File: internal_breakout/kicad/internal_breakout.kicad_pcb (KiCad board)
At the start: 2 copper layers, 50 x 35 mm, 27 parts, among them J1 MA03-1, J10 2X5, J11 2X5, J12 MA03-1, J13 MA03-1, J14 MA03-1, J15 MA03-1, J16 MA03-1, J17 MA03-1, J18 Conn_02x01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

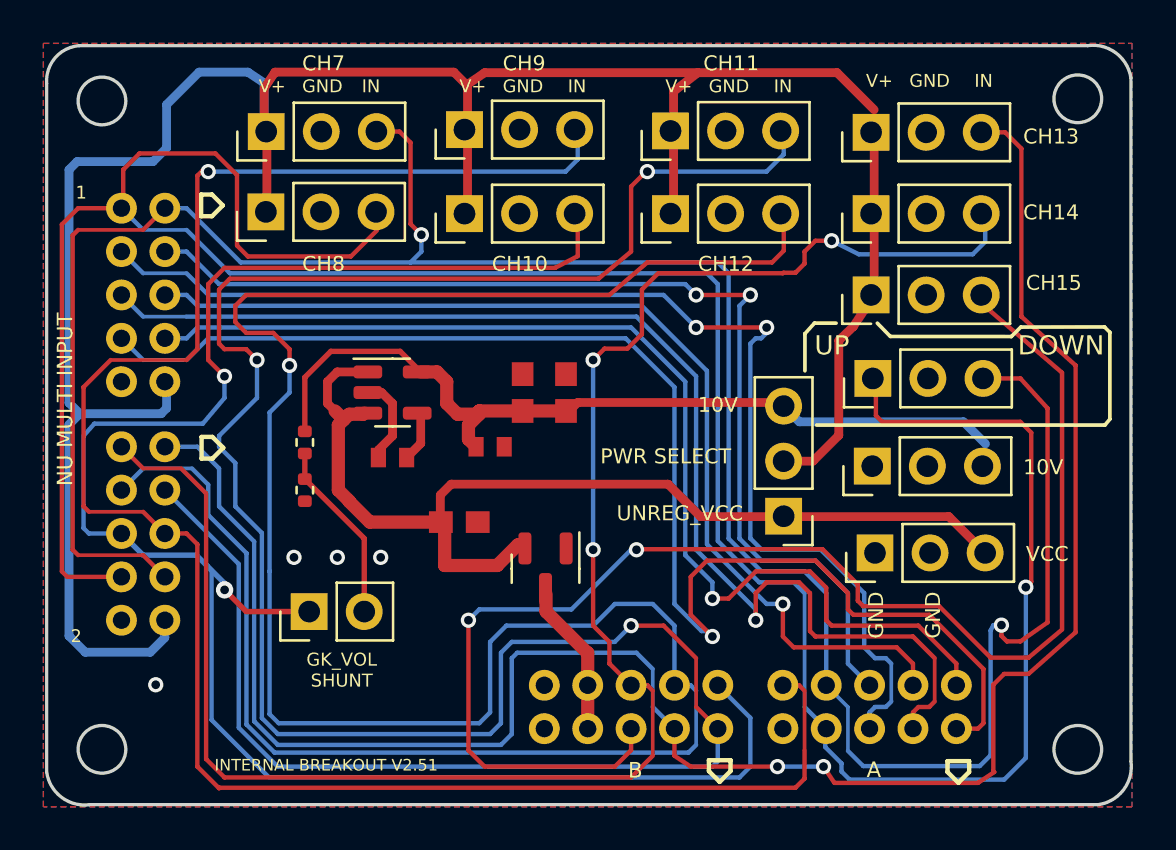
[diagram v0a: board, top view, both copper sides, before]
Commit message: Perfect port to KiCAD
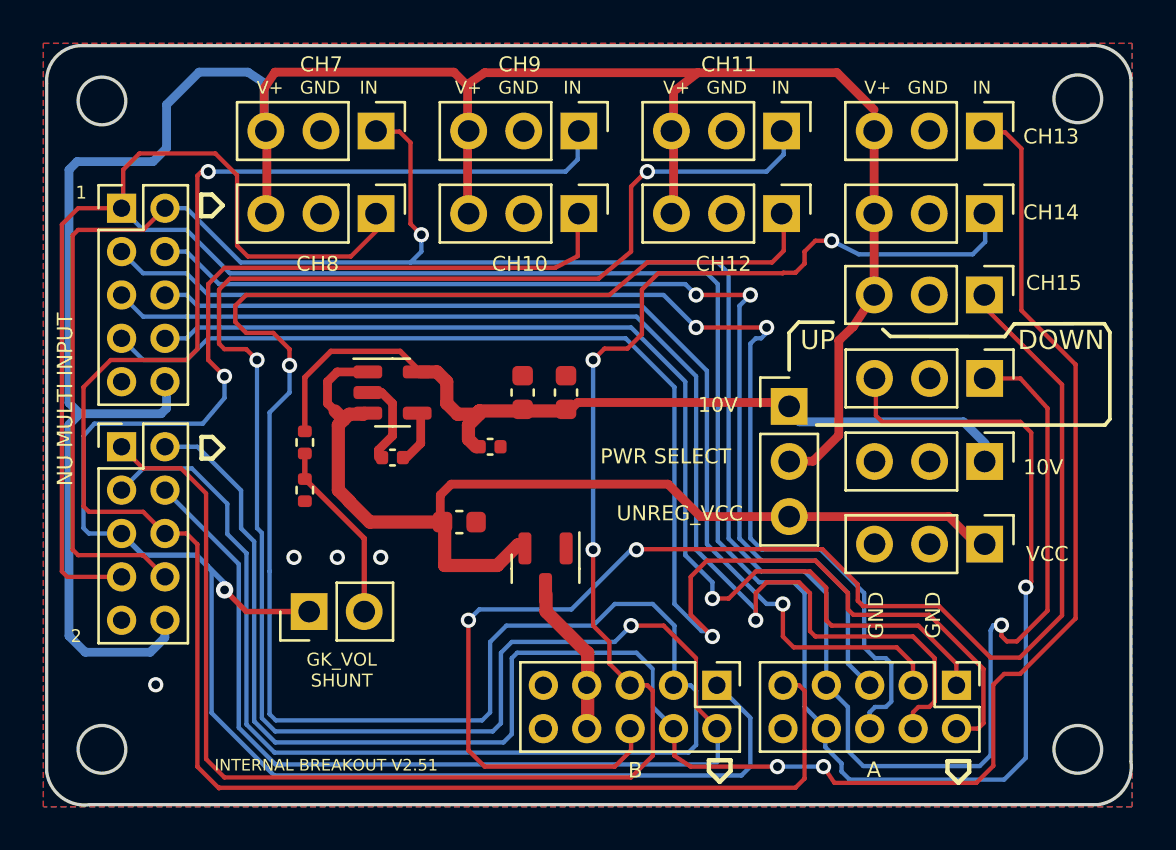
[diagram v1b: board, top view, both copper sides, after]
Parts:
- C1, C2: value C-EUC0603 -> 10uF; footprint internal_breakout:C0603 -> Capacitor_SMD:C_0603_1608Metric
- C3: value C-EUC0603 -> 1uF; footprint internal_breakout:C0603 -> Capacitor_SMD:C_0603_1608Metric
- C4: value C-EUC0402 -> 10nF; footprint internal_breakout:C0402 -> Capacitor_SMD:C_0402_1005Metric
- C5: value C-EUC0402 -> 100nF; footprint internal_breakout:C0402 -> Capacitor_SMD:C_0402_1005Metric
- J10, J11, J3, J4: footprint internal_breakout:2X5 -> Connector_PinHeader_2.00mm:PinHeader_2x05_P2.00mm_Vertical; moved to F.Cu
- J15, J16, J17: value MA03-1 -> Conn_01x03
- R1, R2: value R_Small -> 50K
- U1: value LP2985AIM5-3.3 -> LP2985-10DBVR
- moved J1 5.27 mm to (148.0, 91.4), turned to -90 degrees
- moved J2 5.27 mm to (148.0, 95.2), turned to -90 degrees
- moved J8 5.22 mm to (166.7, 91.4), turned to -90 degrees
- moved J7 5.22 mm to (166.7, 95.2), turned to -90 degrees
- moved J9 5.22 mm to (166.7, 99.0), turned to -90 degrees
- moved J12 5.19 mm to (166.8, 106.7), turned to -90 degrees
- moved J17 5.16 mm to (166.8, 102.8), turned to -90 degrees
- moved J6 5.12 mm to (157.4, 91.4), turned to -90 degrees
- moved J5 5.12 mm to (157.4, 95.2), turned to -90 degrees
- moved J16 5.08 mm to (138.7, 95.2), turned to -90 degrees
- moved J13 5.07 mm to (166.8, 110.5), turned to -90 degrees
- moved J14 5.07 mm to (157.7, 104.1), turned to 0 degrees
- moved J15 5.07 mm to (138.7, 91.4), turned to -90 degrees
- moved J10 4.13 mm to (165.4, 117.0), turned to -90 degrees
- moved J3 4.12 mm to (127.0, 95.0), turned to 0 degrees
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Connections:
- net /CH1 renamed CH2
- net /CH2 renamed CH1
- net /CH3 renamed CH4
- net /CH4 renamed CH3
- net /CH5 renamed CH6
- net /CH6 renamed CH5
- net /VIN renamed VIN
- C1 pad 1: /VCC -> VCC
- C2 pad 1: /+10VA -> +10VA
- C3 pad 1: /+10VA -> +10VA
- C5 pad 1: /+10VA -> +10VA
- J1 pad 1: /V+ -> CH9
- J1 pad 3: /CH9 -> V+
- J10 pad 10: /CH9 -> GND
- J10 pad 7: /CH8 -> CH7
- J10 pad 8: /CH7 -> CH8
- J10 pad 9: GND -> CH9
- J11 pad 1: /CH11 -> CH10
- J11 pad 2: /CH10 -> CH11
- J11 pad 3: /CH13 -> CH12
- J11 pad 4: /CH12 -> CH13
- J11 pad 5: /CH15 -> CH14
- J11 pad 6: /CH14 -> CH15
- J12 pad 1: GND -> +10VA
- J12 pad 3: /+10VA -> GND
- J13 pad 1: GND -> VCC
- J13 pad 3: /VCC -> GND
- J14 pad 1: /VCC -> +10VA
- J14 pad 2: /V+ -> V+
- J14 pad 3: /+10VA -> VCC
- J15 pad 1: /V+ -> CH7
- J15 pad 3: /CH7 -> V+
- J16 pad 1: /V+ -> CH8
- J16 pad 3: /CH8 -> V+
- J17 pad 1: /CH8 -> CH7
- J17 pad 3: /CH7 -> CH8
- J18 pad 1: /CH10 -> CH10
- J2 pad 1: /V+ -> CH10
- J2 pad 3: /CH10 -> V+
- J3 pad 1: /CH7 -> CH8
- J3 pad 10: GND -> V+
- J3 pad 2: /CH8 -> CH7
- J3 pad 9: /V+ -> GND
- J4 pad 1: /CH13 -> CH14
- J4 pad 10: GND -> V+
- J4 pad 2: /CH14 -> CH13
- J4 pad 3: /CH11 -> CH12
- J4 pad 4: /CH12 -> CH11
- J4 pad 5: /CH9 -> CH10
- J4 pad 6: /CH10 -> CH9
- J4 pad 7: /CH7 -> CH8
- J4 pad 8: /CH8 -> CH7
- J4 pad 9: /V+ -> GND
- J5 pad 1: /V+ -> CH12
- J5 pad 3: /CH12 -> V+
- J6 pad 1: /V+ -> CH11
- J6 pad 3: /CH11 -> V+
- J7 pad 1: /V+ -> CH14
- J7 pad 3: /CH14 -> V+
- J8 pad 1: /V+ -> CH13
- J8 pad 3: /CH13 -> V+
- J9 pad 1: /V+ -> CH15
- J9 pad 3: /CH15 -> V+
- Q1 pad 2: /VCC -> VCC
- R1 pad 1: /+10VA -> +10VA
- U1 pad 1: /VCC -> VCC
- U1 pad 3: /VCC -> VCC
- U1 pad 5: /+10VA -> +10VA
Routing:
- net CH8: track 0.00 -> 128.1 mm, vias 0 -> 1
- net /CH8: track 128.1 -> 0.00 mm, vias 1 -> 0
- net /CH11: track 119.4 -> 0.00 mm, vias 3 -> 0
- net CH11: track 0.00 -> 117.8 mm, vias 0 -> 3
- net /CH12: track 116.7 -> 0.00 mm, vias 1 -> 0
- net CH12: track 0.00 -> 116.6 mm, vias 0 -> 1
- net /CH7: track 114.2 -> 0.00 mm, vias 2 -> 0
- net CH7: track 0.00 -> 114.0 mm, vias 0 -> 2
- net V+: track 0.00 -> 113.1 mm
- net /V+: track 113.1 -> 0.00 mm
- net /CH13: track 92.3 -> 0.00 mm, vias 2 -> 0
- net CH13: track 0.00 -> 91.6 mm, vias 0 -> 2
- net CH9: track 0.00 -> 88.7 mm, vias 0 -> 1
- net /CH9: track 88.7 -> 0.00 mm, vias 1 -> 0
- net /CH10: track 86.4 -> 0.00 mm, vias 2 -> 0
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
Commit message: LCSC part numbers
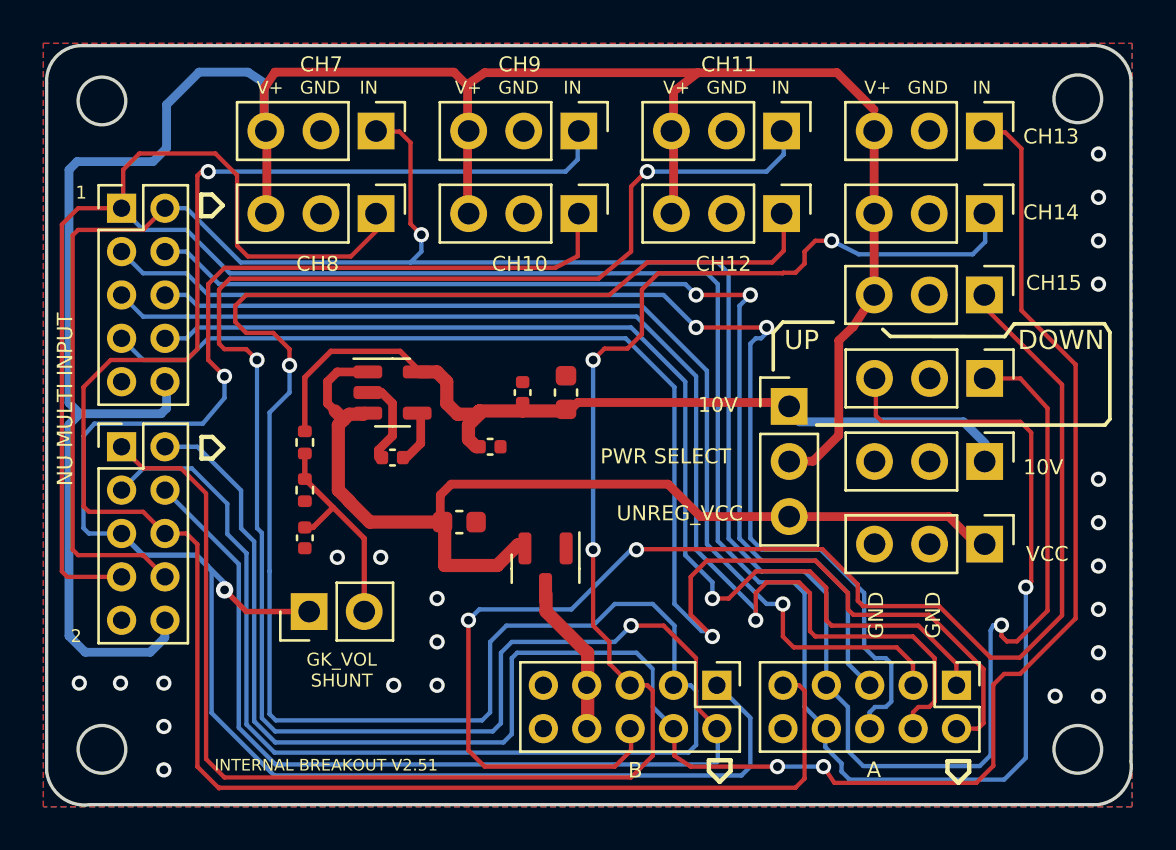
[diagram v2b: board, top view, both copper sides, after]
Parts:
- added C6: 1uF, Capacitor_SMD:C_0402_1005Metric, F.Cu at (135.4, 110.2)
- C3: footprint Capacitor_SMD:C_0603_1608Metric -> Capacitor_SMD:C_0402_1005Metric
- Q1: value FDN360P -> DMP3099L-7
- R1, R2: value 50K -> 47K
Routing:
- net Net-(J18-Pad2): track 8.42 -> 10.1 mm
- net GND: vias 4 -> 22

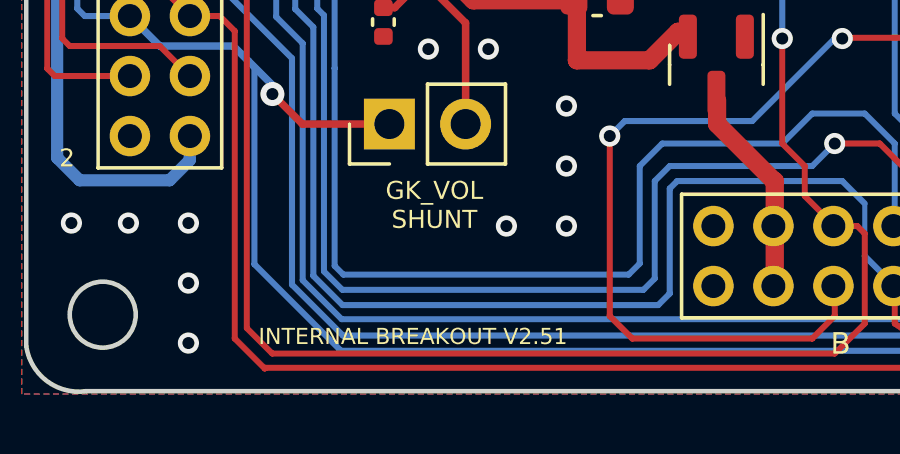
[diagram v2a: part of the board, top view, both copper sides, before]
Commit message: Fixed missing logo
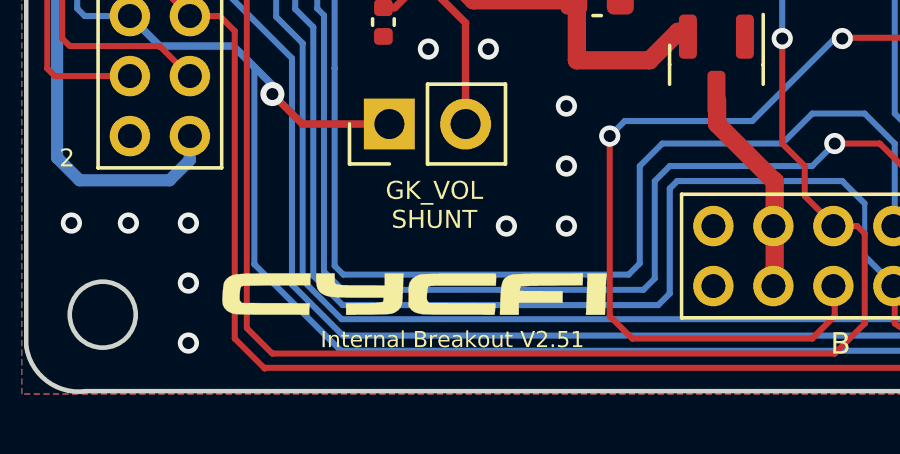
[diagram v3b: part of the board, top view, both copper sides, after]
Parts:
- added G***: LOGO, cycfi_library:cycfi-logo-12mm, F.Cu at (136.4, 119.3)
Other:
- board text added: "Internal Breakout V2.51"
- board text removed: "INTERNAL BREAKOUT V2.51"
